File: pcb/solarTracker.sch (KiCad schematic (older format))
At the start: 25 parts, among them U1 74HC4052, U2 STM32F071CBT6

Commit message: fix step up circuit
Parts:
- removed L?: INDUCTOR, symbol INDUCTOR
- added L?: INDUCTOR, symbol INDUCTOR
- added R?: 180, symbol R
- C?: value 470p -> 1500p
- gave numbers to parts that had none: 2
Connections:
- wire segments 102 -> 141
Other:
- moved on the sheet: 100u, C?, D?, R1, R2

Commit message: debugger circuit
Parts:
- added C?: C, symbol C
- added U?: SWD, symbol SWD
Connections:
- net labels added: SWCLK, SWDCLK, SWDIO, nRST
- wire segments 141 -> 157
- no-connect marks 5 -> 7

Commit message: replace servo with conn
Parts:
- removed S?: Servo, symbol Servo
- added SERVO_Y, SERVO_Z: CONN_01X03, symbol CONN_01X03
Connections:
- net labels added: MULX_ADDR0, MULX_ADDR1, PHOTODIODE, SERVO_Y, SERVO_Z
- wire segments 157 -> 161
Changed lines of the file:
@@
 Order number for the through hole TI chip
-$Comp
-L Servo S?
-U 1 1 55BE7FEA
-P 9750 5450
-F 0 "S?" H 9750 5450 60  0000 C CNN
-F 1 "Servo" H 9750 5450 60  0000 C CNN
-F 2 "" H 9750 5450 60  0000 C CNN
-F 3 "" H 9750 5450 60  0000 C CNN
-	1    9750 5450
-	1    0    0    -1
-$EndComp
 $Comp
 L MC33063A U?
@@
 L +6V #PWR?
 U 1 1 55C135F5
-P 9225 4925
-F 0 "#PWR?" H 9225 4775 50  0001 C CNN
-F 1 "+6V" H 9225 5065 50  0000 C CNN
-F 2 "" H 9225 4925 60  0000 C CNN
-F 3 "" H 9225 4925 60  0000 C CNN
-	1    9225 4925
+P 9775 4025
+F 0 "#PWR?" H 9775 3875 50  0001 C CNN
+F 1 "+6V" H 9775 4165 50  0000 C CNN
+F 2 "" H 9775 4025 60  0000 C CNN
+F 3 "" H 9775 4025 60  0000 C CNN
+	1    9775 4025
 	1    0    0    -1
 $EndComp
@@
 L GND #PWR?
 U 1 1 55C1373F
-P 9225 5350
-F 0 "#PWR?" H 9225 5100 50  0001 C CNN
-F 1 "GND" H 9225 5200 50  0000 C CNN
-F 2 "" H 9225 5350 60  0000 C CNN
-F 3 "" H 9225 5350 60  0000 C CNN
-	1    9225 5350
+P 9775 4350
+F 0 "#PWR?" H 9775 4100 50  0001 C CNN
+F 1 "GND" H 9775 4200 50  0000 C CNN
+F 2 "" H 9775 4350 60  0000 C CNN
+F 3 "" H 9775 4350 60  0000 C CNN
+	1    9775 4350
 	1    0    0    -1
 $EndComp
@@
 	4500 2150 4500 2375
 Wire Wire Line
-	9225 5300 9300 5300
-Wire Wire Line
-	9225 5350 9225 5300
-Wire Wire Line
-	9225 5000 9300 5000
-Wire Wire Line
-	9225 4925 9225 5000
+	9775 4300 9850 4300
+Wire Wire Line
+	9775 4350 9775 4300
+Wire Wire Line
+	9775 4100 9850 4100
+Wire Wire Line
+	9775 4025 9775 4100
 Wire Wire Line
 	7950 2325 8475 2325
@@
 Text Label 8300 4500 0    60   ~ 0
 SWCLK
+Text Label 5900 5200 0    60   ~ 0
+MULX_ADDR0
+Text Label 5900 5350 0    60   ~ 0
+MULX_ADDR1
+Text Label 5900 5500 0    60   ~ 0
+PHOTODIODE
+Text Label 5900 5625 0    60   ~ 0
+SERVO_Z
+$Comp
+L CONN_01X03 SERVO_Y
+U 1 1 55CEE6B6
+P 10050 4200
+F 0 "SERVO_Y" H 10050 4400 50  0000 C CNN
+F 1 "CONN_01X03" H 10125 3975 50  0000 C CNN
+F 2 "" H 10050 4200 60  0000 C CNN
+F 3 "" H 10050 4200 60  0000 C CNN
+	1    10050 4200
+	1    0    0    -1
+$EndComp
+$Comp
+L +6V #PWR?
+U 1 1 55CEE86D
+P 9775 4925
+F 0 "#PWR?" H 9775 4775 50  0001 C CNN
+F 1 "+6V" H 9775 5065 50  0000 C CNN
+F 2 "" H 9775 4925 60  0000 C CNN
+F 3 "" H 9775 4925 60  0000 C CNN
+	1    9775 4925
+	1    0    0    -1
+$EndComp
+$Comp
+L GND #PWR?
+U 1 1 55CEE873
+P 9775 5250
+F 0 "#PWR?" H 9775 5000 50  0001 C CNN
+F 1 "GND" H 9775 5100 50  0000 C CNN
+F 2 "" H 9775 5250 60  0000 C CNN
+F 3 "" H 9775 5250 60  0000 C CNN
+	1    9775 5250
+	1    0    0    -1
+$EndComp
+Wire Wire Line
+	9775 5200 9850 5200
+Wire Wire Line
+	9775 5250 9775 5200
+Wire Wire Line
+	9775 5000 9850 5000
+Wire Wire Line
+	9775 4925 9775 5000
+$Comp
+L CONN_01X03 SERVO_Z
+U 1 1 55CEE87D
+P 10050 5100
+F 0 "SERVO_Z" H 10050 5300 50  0000 C CNN
+F 1 "CONN_01X03" H 10100 4850 50  0000 C CNN
+F 2 "" H 10050 5100 60  0000 C CNN
+F 3 "" H 10050 5100 60  0000 C CNN
+	1    10050 5100
+	1    0    0    -1
+$EndComp
+Text Label 5900 5775 0    60   ~ 0
+SERVO_Y
 $EndSCHEMATC

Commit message: lm2577 regulator for 6V supply
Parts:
- removed 100u: CP, symbol CP
- removed C?: 470u, symbol CP
- removed C?: 1500p, symbol C
- removed D?: 1N5819, symbol D_Schottky
- removed L?: INDUCTOR, symbol INDUCTOR
- removed R1: 68k, symbol R
- removed R2: 18k, symbol R
- removed R?: 180, symbol R
- removed U?: MC33063A, symbol MC33063A
- added C?: 100n, symbol C
- added C?: 270n, symbol C
- added C?: 2000µ, symbol CP
- added D?: D_Schottky, symbol D_Schottky
- added L?: 47µ, symbol INDUCTOR
- added R?: 2k7, symbol R
- added R? (x2): R, symbol R
- added U?: LM2577, symbol LM2577
- C?: value C -> 100n
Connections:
- wire segments 161 -> 116
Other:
- note added: "Need a level shifter here\n"
- note removed: "vo = 1.25(1+ R2/R1)"
- moved on the sheet: C?, U?

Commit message: some farnell codes
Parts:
- C?: Farnell Code (none) -> 1854883
- C?: Farnell Code (none) -> 1890582
- R?: value R -> 62k
- R?: value R -> 16k
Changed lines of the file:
@@
 P 6900 2375
 F 0 "U?" H 6900 2375 60  0000 C CNN
-F 1 "LM2577" H 6900 2375 60  0000 C CNN
+F 1 "LM2577" H 7100 2600 60  0000 C CNN
 F 2 "" H 6900 2375 60  0000 C CNN
 F 3 "" H 6900 2375 60  0000 C CNN
@@
 F 2 "" H 6113 2200 30  0000 C CNN
 F 3 "" H 6075 2350 60  0000 C CNN
+F 4 "1854883" H 6075 2350 60  0001 C CNN "Farnell Code"
 	1    6075 2350
 	1    0    0    -1
@@
 F 2 "" H 8238 1925 30  0000 C CNN
 F 3 "" H 8200 2075 60  0000 C CNN
+F 4 "1890582" H 8200 2075 60  0001 C CNN "Farnell Code"
 	1    8200 2075
 	1    0    0    -1
@@
 P 7925 1400
 F 0 "R?" V 8005 1400 50  0000 C CNN
-F 1 "R" V 7925 1400 50  0000 C CNN
+F 1 "62k" V 7925 1400 50  0000 C CNN
 F 2 "" V 7855 1400 30  0000 C CNN
 F 3 "" H 7925 1400 30  0000 C CNN
@@
 P 7925 2075
 F 0 "R?" V 8005 2075 50  0000 C CNN
-F 1 "R" V 7925 2075 50  0000 C CNN
+F 1 "16k" V 7925 2075 50  0000 C CNN
 F 2 "" V 7855 2075 30  0000 C CNN
 F 3 "" H 7925 2075 30  0000 C CNN

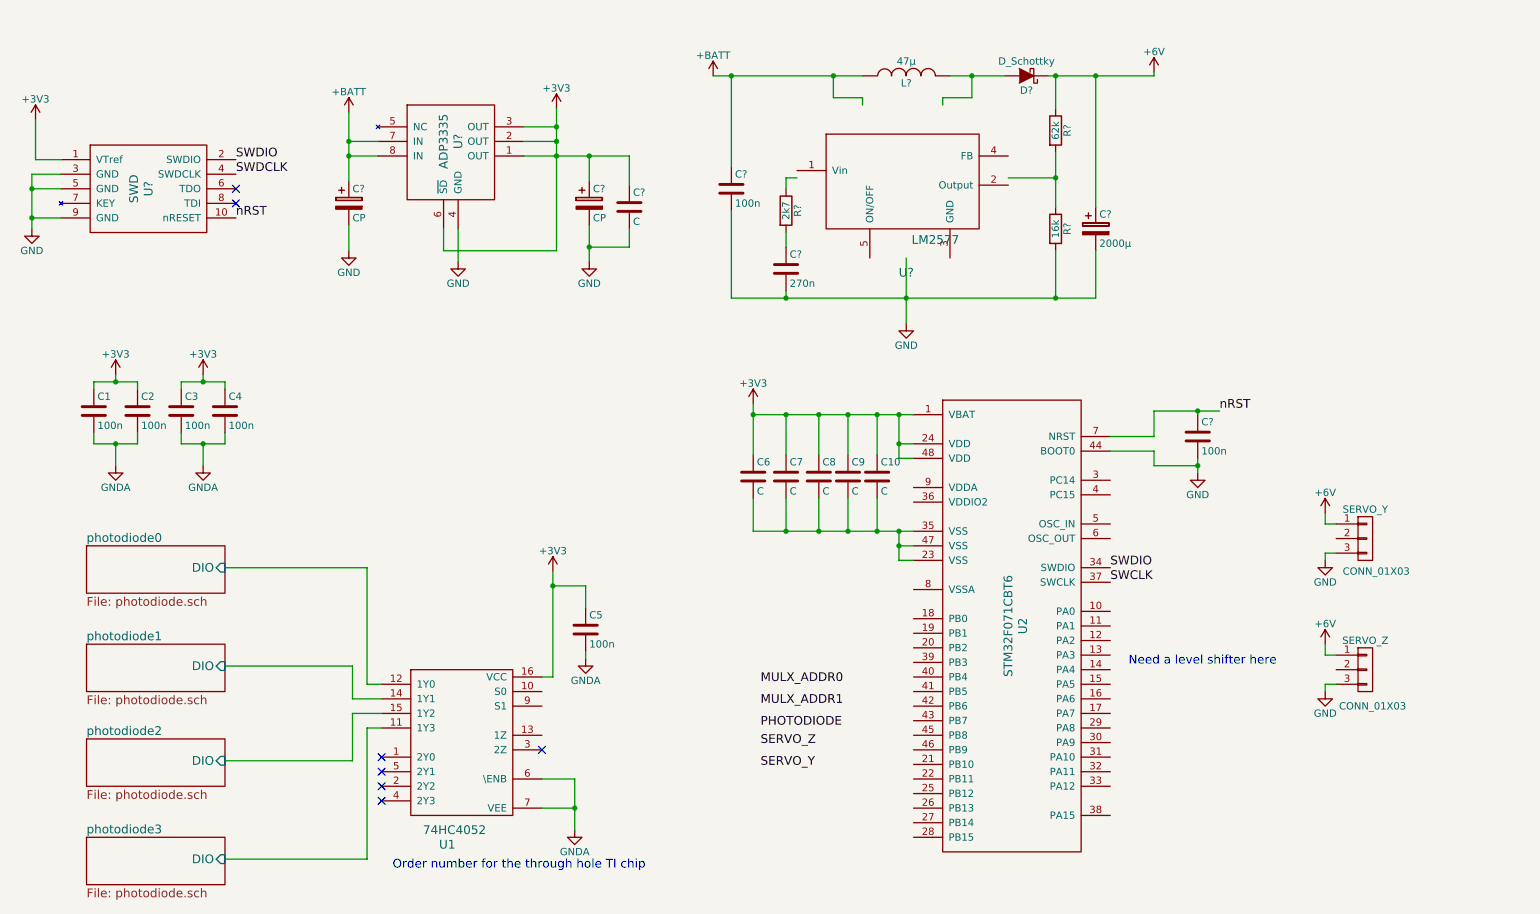
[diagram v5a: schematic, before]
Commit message: switch to LM2596 step down converter, Vbatt to be 9V alkaline
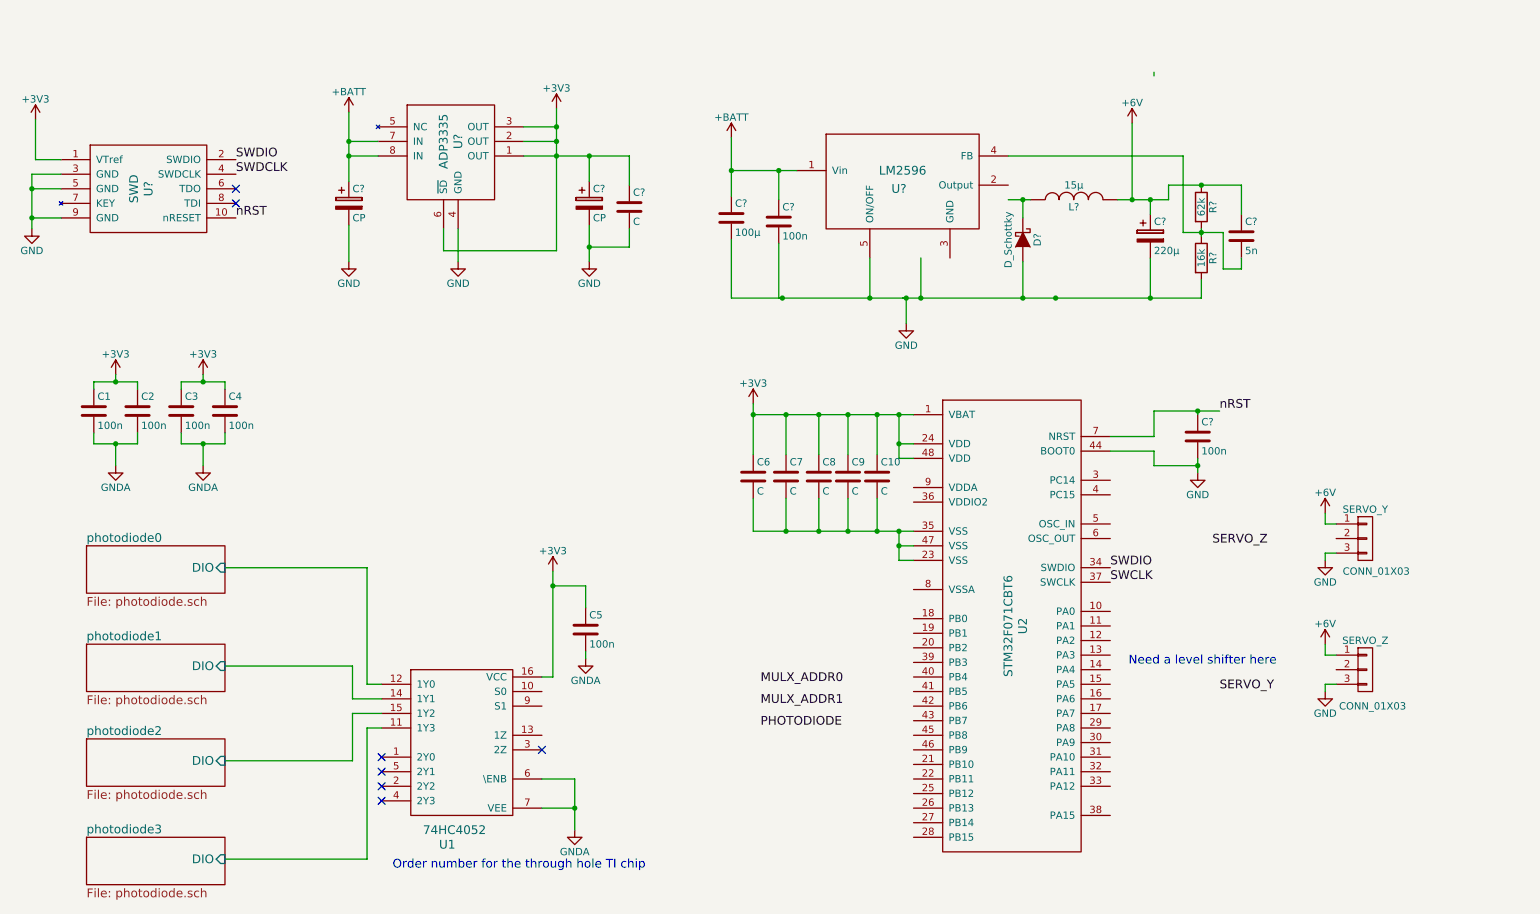
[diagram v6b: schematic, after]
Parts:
- removed C?: 270n, symbol C
- removed L?: 47µ, symbol INDUCTOR
- removed R?: 2k7, symbol R
- added C?: 5n, symbol C
- added C?: 100n, symbol C
- added L?: 15µ, symbol INDUCTOR
- C?: value 100n -> 100µ
- C?: value 2000µ -> 220µ
- U?: value LM2577 -> LM2596
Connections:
- wire segments 116 -> 122
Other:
- moved on the sheet: C?, D?, R?
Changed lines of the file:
@@
 L GND #PWR?
 U 1 1 55C159D0
-P 3075 2225
-F 0 "#PWR?" H 3075 1975 50  0001 C CNN
-F 1 "GND" H 3075 2075 50  0000 C CNN
-F 2 "" H 3075 2225 60  0000 C CNN
-F 3 "" H 3075 2225 60  0000 C CNN
-	1    3075 2225
+P 3075 2300
+F 0 "#PWR?" H 3075 2050 50  0001 C CNN
+F 1 "GND" H 3075 2150 50  0000 C CNN
+F 2 "" H 3075 2300 60  0000 C CNN
+F 3 "" H 3075 2300 60  0000 C CNN
+	1    3075 2300
 	1    0    0    -1
 $EndComp
@@
 Text Label 5900 5500 0    60   ~ 0
 PHOTODIODE
-Text Label 5900 5625 0    60   ~ 0
+Text Label 9000 4250 0    60   ~ 0
 SERVO_Z
 $Comp
@@
 	1    0    0    -1
 $EndComp
-Text Label 5900 5775 0    60   ~ 0
+Text Label 9050 5250 0    60   ~ 0
 SERVO_Y
 Text Notes 8425 5075 0    60   ~ 0
@@
 U 1 1 55E0DA21
 P 6900 2375
-F 0 "U?" H 6900 2375 60  0000 C CNN
-F 1 "LM2577" H 7100 2600 60  0000 C CNN
+F 0 "U?" H 6850 2950 60  0000 C CNN
+F 1 "LM2596" H 6875 3075 60  0000 C CNN
 F 2 "" H 6900 2375 60  0000 C CNN
 F 3 "" H 6900 2375 60  0000 C CNN
@@
 L +BATT #PWR?
 U 1 1 55E0DBC4
-P 5575 1025
-F 0 "#PWR?" H 5575 875 50  0001 C CNN
-F 1 "+BATT" H 5575 1165 50  0000 C CNN
-F 2 "" H 5575 1025 60  0000 C CNN
-F 3 "" H 5575 1025 60  0000 C CNN
-	1    5575 1025
-	1    0    0    -1
-$EndComp
-$Comp
-L INDUCTOR L?
-U 1 1 55E0E00A
-P 6900 1025
-F 0 "L?" V 6850 1025 50  0000 C CNN
-F 1 "47µ" V 7000 1025 50  0000 C CNN
-F 2 "" H 6900 1025 60  0000 C CNN
-F 3 "" H 6900 1025 60  0000 C CNN
-	1    6900 1025
-	0    -1   -1   0
+P 5700 1450
+F 0 "#PWR?" H 5700 1300 50  0001 C CNN
+F 1 "+BATT" H 5700 1590 50  0000 C CNN
+F 2 "" H 5700 1450 60  0000 C CNN
+F 3 "" H 5700 1450 60  0000 C CNN
+	1    5700 1450
+	1    0    0    -1
 $EndComp
 $Comp
 L D_Schottky D?
 U 1 1 55E0E96D
-P 7725 1025
-F 0 "D?" H 7725 1125 50  0000 C CNN
-F 1 "D_Schottky" H 7725 925 50  0000 C CNN
-F 2 "" H 7725 1025 60  0000 C CNN
-F 3 "" H 7725 1025 60  0000 C CNN
-	1    7725 1025
-	-1   0    0    1
+P 7700 2150
+F 0 "D?" H 7700 2250 50  0000 C CNN
+F 1 "D_Schottky" H 7700 2050 50  0000 C CNN
+F 2 "" H 7700 2150 60  0000 C CNN
+F 3 "" H 7700 2150 60  0000 C CNN
+	1    7700 2150
+	0    1    1    0
 $EndComp
 $Comp
 L C C?
 U 1 1 55E0F064
-P 5700 1800
-F 0 "C?" H 5725 1900 50  0000 L CNN
-F 1 "100n" H 5725 1700 50  0000 L CNN
-F 2 "" H 5738 1650 30  0000 C CNN
-F 3 "" H 5700 1800 60  0000 C CNN
-	1    5700 1800
+P 5700 2000
+F 0 "C?" H 5725 2100 50  0000 L CNN
+F 1 "100µ" H 5725 1900 50  0000 L CNN
+F 2 "" H 5738 1850 30  0000 C CNN
+F 3 "" H 5700 2000 60  0000 C CNN
+	1    5700 2000
 	1    0    0    -1
 $EndComp
@@
 $EndComp
 $Comp
-L R R?
-U 1 1 55E0F5EF
-P 6075 1950
-F 0 "R?" V 6155 1950 50  0000 C CNN
-F 1 "2k7" V 6075 1950 50  0000 C CNN
-F 2 "" V 6005 1950 30  0000 C CNN
-F 3 "" H 6075 1950 30  0000 C CNN
-	1    6075 1950
-	1    0    0    -1
-$EndComp
-$Comp
-L C C?
-U 1 1 55E0F6BF
-P 6075 2350
-F 0 "C?" H 6100 2450 50  0000 L CNN
-F 1 "270n" H 6100 2250 50  0000 L CNN
-F 2 "" H 6113 2200 30  0000 C CNN
-F 3 "" H 6075 2350 60  0000 C CNN
-F 4 "1854883" H 6075 2350 60  0001 C CNN "Farnell Code"
-	1    6075 2350
-	1    0    0    -1
-$EndComp
-$Comp
 L CP C?
 U 1 1 55E10453
-P 8200 2075
-F 0 "C?" H 8225 2175 50  0000 L CNN
-F 1 "2000µ" H 8225 1975 50  0000 L CNN
-F 2 "" H 8238 1925 30  0000 C CNN
-F 3 "" H 8200 2075 60  0000 C CNN
-F 4 "1890582" H 8200 2075 60  0001 C CNN "Farnell Code"
-	1    8200 2075
+P 8575 2125
+F 0 "C?" H 8600 2225 50  0000 L CNN
+F 1 "220µ" H 8600 2025 50  0000 L CNN
+F 2 "" H 8613 1975 30  0000 C CNN
+F 3 "" H 8575 2125 60  0000 C CNN
+F 4 "1890582" H 8575 2125 60  0001 C CNN "Farnell Code"
+	1    8575 2125
 	1    0    0    -1
 $EndComp
@@
 L +6V #PWR?
 U 1 1 55E10A05
-P 8600 1000
-F 0 "#PWR?" H 8600 850 50  0001 C CNN
-F 1 "+6V" H 8600 1140 50  0000 C CNN
-F 2 "" H 8600 1000 60  0000 C CNN
-F 3 "" H 8600 1000 60  0000 C CNN
-	1    8600 1000
+P 8450 1350
+F 0 "#PWR?" H 8450 1200 50  0001 C CNN
+F 1 "+6V" H 8450 1490 50  0000 C CNN
+F 2 "" H 8450 1350 60  0000 C CNN
+F 3 "" H 8450 1350 60  0000 C CNN
+	1    8450 1350
 	1    0    0    -1
 $EndComp
@@
 L R R?
 U 1 1 55E114F9
-P 7925 1400
-F 0 "R?" V 8005 1400 50  0000 C CNN
-F 1 "62k" V 7925 1400 50  0000 C CNN
-F 2 "" V 7855 1400 30  0000 C CNN
-F 3 "" H 7925 1400 30  0000 C CNN
-	1    7925 1400
+P 8925 1925
+F 0 "R?" V 9005 1925 50  0000 C CNN
+F 1 "62k" V 8925 1925 50  0000 C CNN
+F 2 "" V 8855 1925 30  0000 C CNN
+F 3 "" H 8925 1925 30  0000 C CNN
+	1    8925 1925
 	1    0    0    -1
 $EndComp
@@
 L R R?
 U 1 1 55E115AC
-P 7925 2075
-F 0 "R?" V 8005 2075 50  0000 C CNN
-F 1 "16k" V 7925 2075 50  0000 C CNN
-F 2 "" V 7855 2075 30  0000 C CNN
-F 3 "" H 7925 2075 30  0000 C CNN
-	1    7925 2075
-	1    0    0    -1
-$EndComp
-Wire Wire Line
-	3075 2050 3075 2225
+P 8925 2275
+F 0 "R?" V 9005 2275 50  0000 C CNN
+F 1 "16k" V 8925 2275 50  0000 C CNN
+F 2 "" V 8855 2275 30  0000 C CNN
+F 3 "" H 8925 2275 30  0000 C CNN
+	1    8925 2275
+	1    0    0    -1
+$EndComp
+Wire Wire Line
+	3075 2050 3075 2300
 Connection ~ 3075 1575
 Connection ~ 4725 2200
@@
 	9775 4925 9775 5000
 Wire Wire Line
-	7150 1175 7150 1225
-Wire Wire Line
-	7150 1175 7350 1175
-Wire Wire Line
-	7350 1175 7350 1025
-Wire Wire Line
-	7200 1025 7575 1025
-Wire Wire Line
-	5575 1025 6600 1025
-Wire Wire Line
-	6600 1225 6600 1175
-Wire Wire Line
-	6600 1175 6400 1175
-Wire Wire Line
-	6400 1175 6400 1025
-Connection ~ 6400 1025
-Connection ~ 7350 1025
-Wire Wire Line
-	7875 1025 8600 1025
-Wire Wire Line
-	5700 1025 5700 1650
-Connection ~ 5700 1025
-Wire Wire Line
-	5700 1950 5700 2550
-Wire Wire Line
-	5700 2550 8200 2550
-Wire Wire Line
-	6900 2275 6900 2725
+	5700 2550 8925 2550
 Connection ~ 6900 2550
 Wire Wire Line
-	6150 1725 6075 1725
-Wire Wire Line
-	6075 1725 6075 1800
-Wire Wire Line
-	6075 2100 6075 2200
-Wire Wire Line
-	6075 2500 6075 2550
-Connection ~ 6075 2550
-Connection ~ 7925 1025
-Wire Wire Line
-	8200 1025 8200 1925
-Connection ~ 8200 1025
-Wire Wire Line
-	8200 2550 8200 2225
-Wire Wire Line
 	8600 1025 8600 1000
-Wire Wire Line
-	7600 1725 7925 1725
-Wire Wire Line
-	7925 1550 7925 1925
-Connection ~ 7925 1725
-Wire Wire Line
-	7925 2225 7925 2550
 Connection ~ 7925 2550
 Wire Wire Line
-	7925 1025 7925 1250
+	5700 1450 5700 1850
+Wire Wire Line
+	5700 2150 5700 2550
+Wire Wire Line
+	5700 1675 6150 1675
+Connection ~ 5700 1675
+Wire Wire Line
+	6650 2275 6650 2550
+Connection ~ 6650 2550
+Wire Wire Line
+	7000 2275 7000 2550
+Connection ~ 7000 2550
+Wire Wire Line
+	6875 2550 6900 2550
+Wire Wire Line
+	6900 2550 6900 2725
+$Comp
+L INDUCTOR L?
+U 1 1 586F1B50
+P 8050 1875
+F 0 "L?" V 8000 1875 50  0000 C CNN
+F 1 "15µ" V 8150 1875 50  0000 C CNN
+F 2 "" H 8050 1875 50  0000 C CNN
+F 3 "" H 8050 1875 50  0000 C CNN
+	1    8050 1875
+	0    -1   -1   0
+$EndComp
+Wire Wire Line
+	8350 1875 8700 1875
+Wire Wire Line
+	8700 1875 8700 1775
+Wire Wire Line
+	8700 1775 9200 1775
+Wire Wire Line
+	8575 1875 8575 1975
+Connection ~ 8575 1875
+Wire Wire Line
+	8575 2550 8575 2275
+Wire Wire Line
+	8925 2550 8925 2425
+Connection ~ 8575 2550
+Wire Wire Line
+	8925 2075 8925 2125
+Wire Wire Line
+	9200 1775 9200 1975
+Connection ~ 8925 1775
+$Comp
+L C C?
+U 1 1 586F29AB
+P 9200 2125
+F 0 "C?" H 9225 2225 50  0000 L CNN
+F 1 "5n" H 9225 2025 50  0000 L CNN
+F 2 "" H 9238 1975 50  0000 C CNN
+F 3 "" H 9200 2125 50  0000 C CNN
+	1    9200 2125
+	1    0    0    -1
+$EndComp
+Wire Wire Line
+	8800 2100 9075 2100
+Wire Wire Line
+	9075 2100 9075 2350
+Wire Wire Line
+	9075 2350 9200 2350
+Wire Wire Line
+	9200 2350 9200 2275
+Connection ~ 8925 2100
+Wire Wire Line
+	7600 1875 7750 1875
+Wire Wire Line
+	7700 1875 7700 2000
+Connection ~ 7700 1875
+Wire Wire Line
+	7700 2300 7700 2550
+Connection ~ 7700 2550
+Wire Wire Line
+	8800 2100 8800 1575
+Wire Wire Line
+	8800 1575 7600 1575
+$Comp
+L C C?
+U 1 1 586F36FD
+P 6025 2025
+F 0 "C?" H 6050 2125 50  0000 L CNN
+F 1 "100n" H 6050 1925 50  0000 L CNN
+F 2 "" H 6063 1875 50  0000 C CNN
+F 3 "" H 6025 2025 50  0000 C CNN
+	1    6025 2025
+	1    0    0    -1
+$EndComp
+Wire Wire Line
+	6025 1675 6025 1875
+Connection ~ 6025 1675
+Wire Wire Line
+	6025 2175 6025 2550
+Wire Wire Line
+	6025 2550 6050 2550
+Connection ~ 6050 2550
+Wire Wire Line
+	8450 1350 8450 1875
+Connection ~ 8450 1875
 $EndSCHEMATC
